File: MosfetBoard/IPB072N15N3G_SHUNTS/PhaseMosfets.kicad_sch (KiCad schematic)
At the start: 26 parts, among them J1 DRIVER1, J4 PhaseConn, Q1 IPB072N15N3G, Q2 IPB072N15N3G, Q4 IPB072N15N3G, Q5 IPB072N15N3G

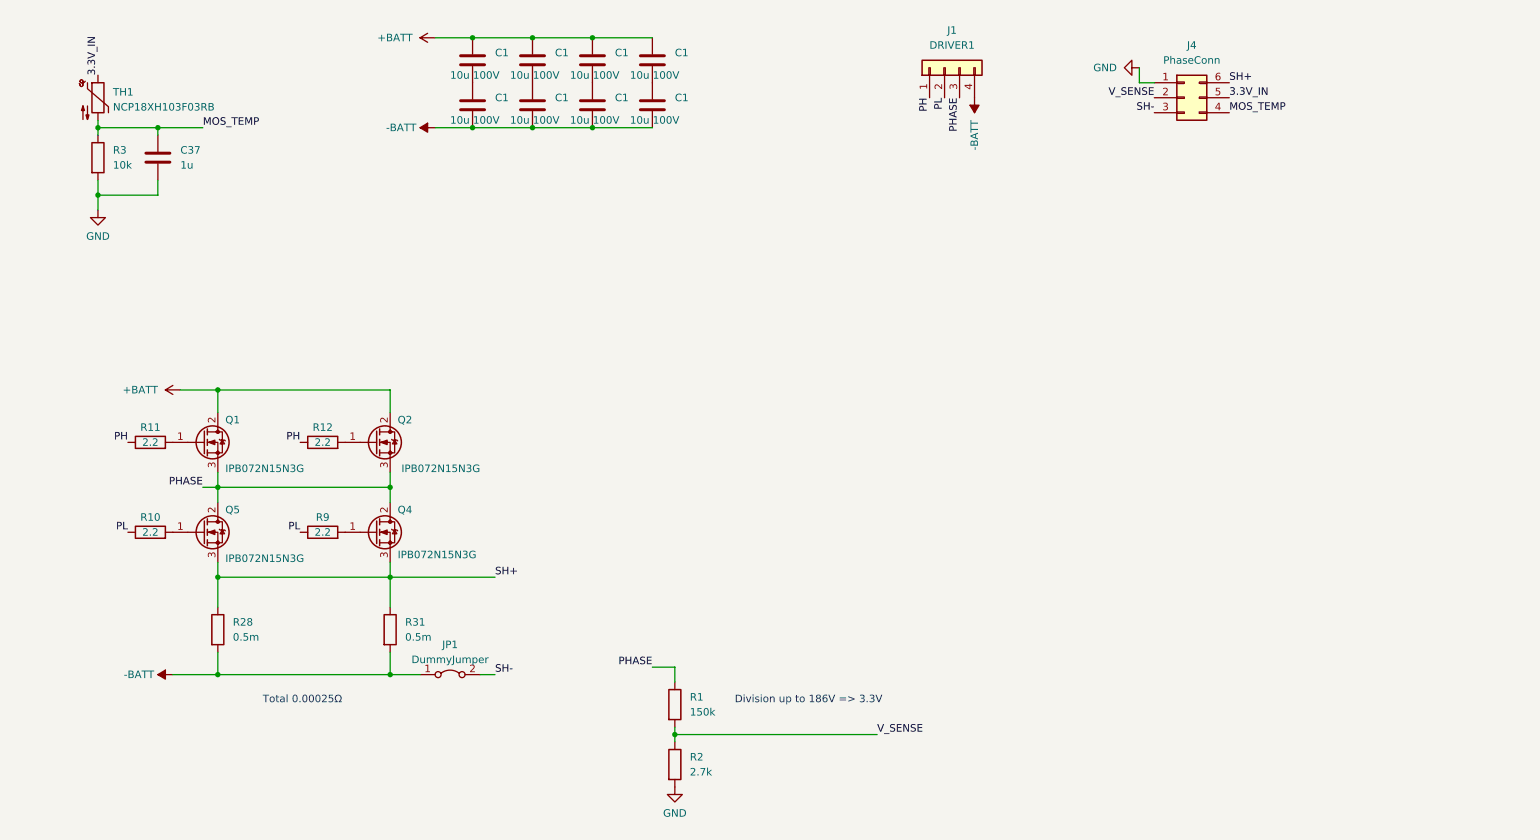
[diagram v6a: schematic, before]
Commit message: v2.8.0 - Small Hall sensors
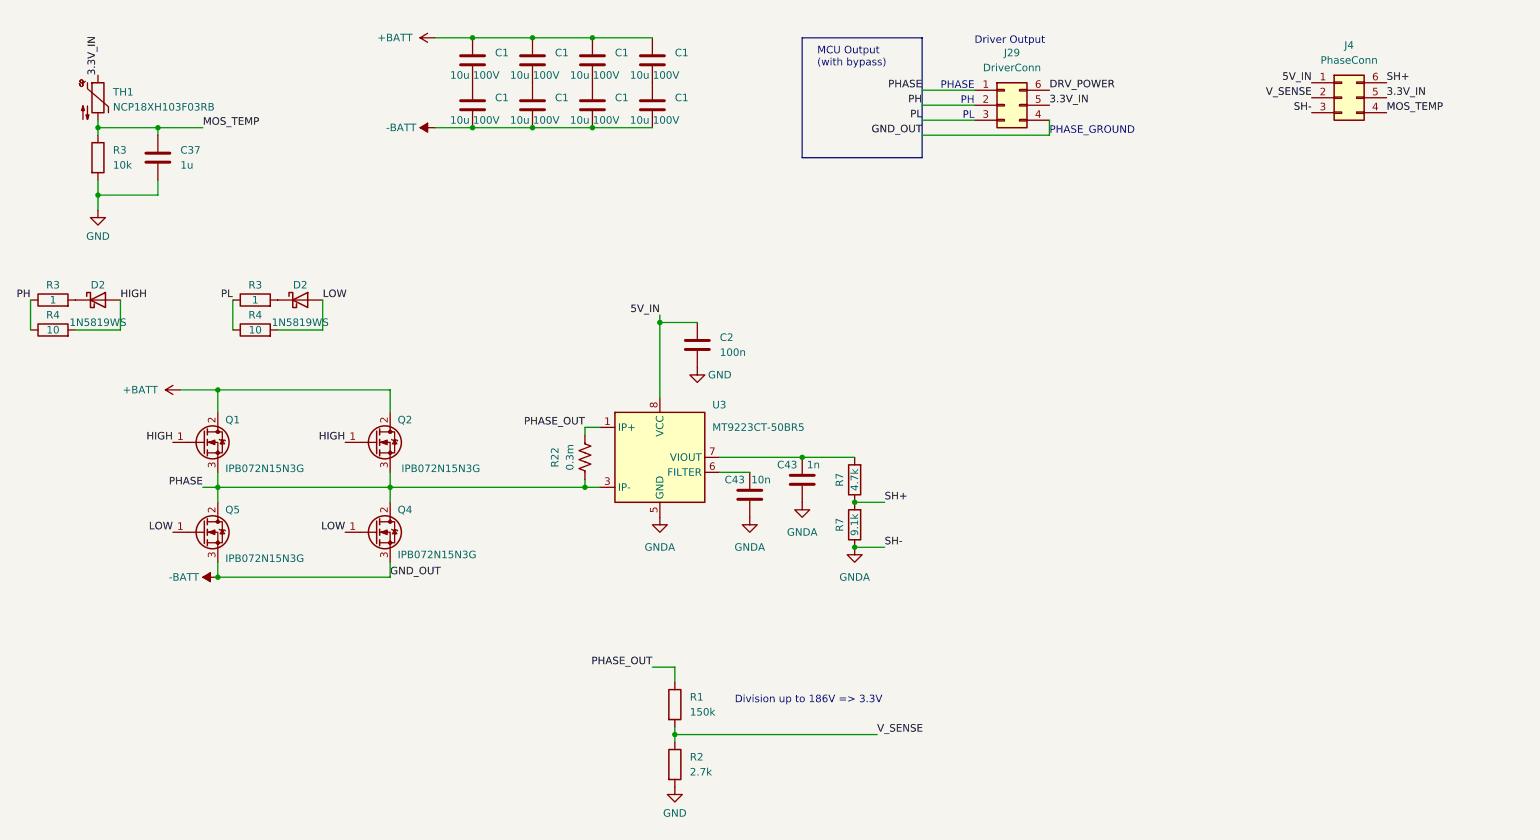
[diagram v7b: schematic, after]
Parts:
- removed J1: DRIVER1, Connector_PinSocket_2.54mm:PinSocket_2x02_P2.54mm_Vertical_SMD, symbol Connector_Generic:Conn_01x04
- removed JP1: DummyJumper, GigaVescLibs:SolderJumper0.3mm, symbol Jumper:Jumper_2_Bridged
- removed R10, R11, R12, R9: 2.2, Resistor_SMD:R_0603_1608Metric, symbol Device:R
- removed R28, R31: 0.5m, Resistor_SMD:R_2512_6332Metric, symbol Device:R
- added C2: 100n, GigaVescLibs:C_0603_1608Metric_L, symbol Device:C
- added C43: 10n, GigaVescLibs:C_0603_1608Metric_L, symbol Device:C
- added C43: 1n, GigaVescLibs:C_0603_1608Metric_L, symbol Device:C
- added D2 (x2): 1N5819WS, Diode_SMD:D_SOD-323, symbol Device:D_Schottky
- added J29: DriverConn, Connector_PinSocket_2.54mm:PinSocket_2x03_P2.54mm_Vertical_SMD, symbol Connector_Generic:Conn_02x03_Counter_Clockwise
- added R22: 0.3m, Resistor_SMD:R_2512_6332Metric, symbol Device:R_US
- added R3 (x2): 1, Resistor_SMD:R_0603_1608Metric, symbol Device:R
- added R4 (x2): 10, Resistor_SMD:R_0603_1608Metric, symbol Device:R
- added R7: 4.7k, Resistor_SMD:R_0603_1608Metric, symbol Device:R
- added R7: 9.1k, Resistor_SMD:R_0603_1608Metric, symbol Device:R
- added U3: MT9223CT-50BR5, Package_SO:SOP-8_3.9x4.9mm_P1.27mm, symbol Sensor_Current:ACS725xLCTR-50AB
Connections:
- net -BATT: now also Q4.3 (S), Q5.3 (S), J29.4 (Pin_4)
- net 3.3V_IN: now also J29.5 (Pin_5)
- net GND: now also C2.1; no longer J4.1 (Pin_1)
- net PH: now also J29.2 (Pin_2), R3.1, R4.1
- net PHASE: now also J29.1 (Pin_1), R22.1, U3.3 (IP-), U3.4 (IP-); no longer R1.1
- net PL: now also J29.3 (Pin_3), R3.1, R4.1
- net SH+: now also R7.1, R7.2; no longer Q4.3 (S), Q5.3 (S)
- net LOW: now reaches Q5.1 (G)
- net LOW: now also Q4.1 (G), D2.2 (A), R4.2
- net HIGH: now reaches Q2.1 (G)
- net HIGH: now also Q1.1 (G), D2.2 (A), R4.2
- net SH- renamed GNDA
- net GNDA: now also C43.2, C43.2, R7.1, U3.5 (GND)
- new net: D2.1 (K), R3.2 (x2)
- new net: C43.1, R7.2, U3.7 (VIOUT)
- new net: C43.1, U3.6 (FILTER)
- new net 5V_IN: C2.2, J4.1 (Pin_1), U3.8 (VCC)
- new net DRV_POWER: J29.6 (Pin_6)
- new net PHASE_OUT: R1.1, R22.2, U3.1 (IP+), U3.2 (IP+)
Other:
- note added: "Driver Output"
- note added: "MCU Output (with bypass)"
- note added: "PH"
- note added: "PHASE"
- note added: "PHASE_GROUND"
- note added: "PL"
- note removed: "Total 0.00025Ω"
- moved on the sheet: J4

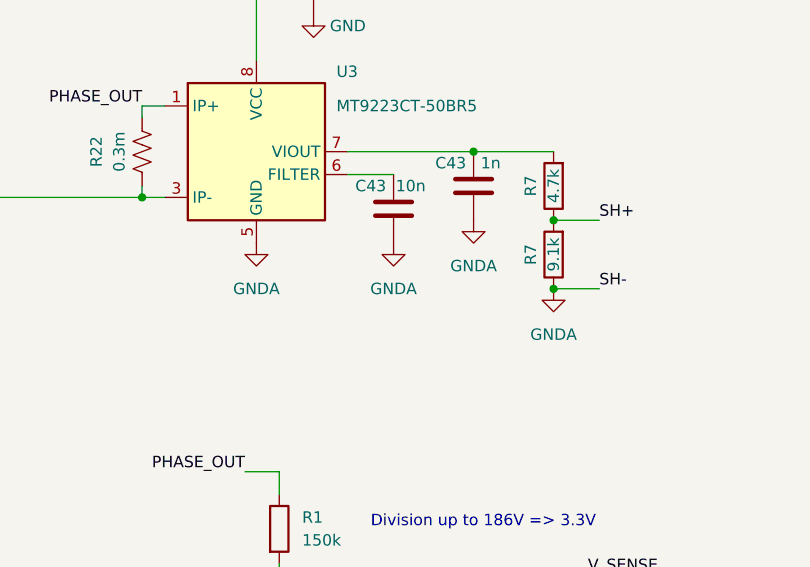
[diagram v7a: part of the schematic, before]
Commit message: v2.8.0 - Small Hall sensors
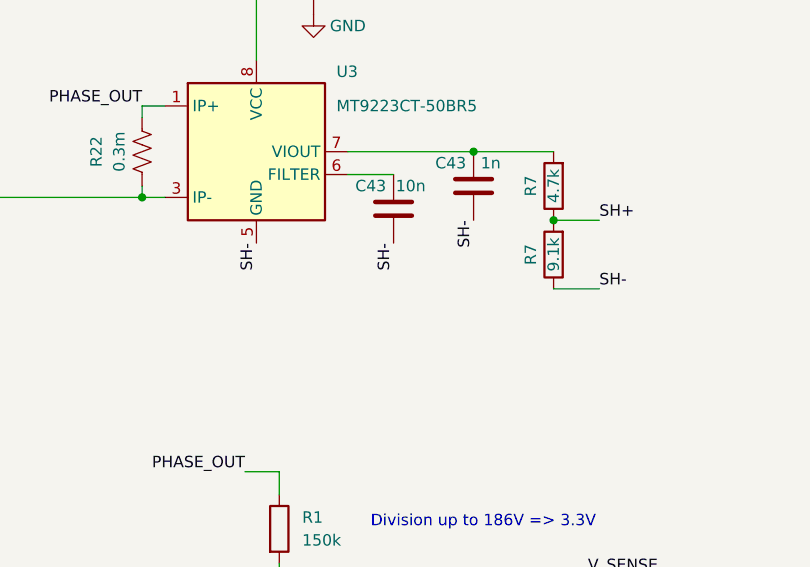
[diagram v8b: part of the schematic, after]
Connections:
- net GNDA renamed SH-
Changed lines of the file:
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@@
   (junction (at 55.88 102.87) (diameter 0) (color 0 0 0 0)
-  )
-  (junction (at 163.83 113.03) (diameter 0) (color 0 0 0 0)
   )
   (junction (at 133.35 144.78) (diameter 0) (color 0 0 0 0)
@@
     (effects (font (size 1.27 1.27)) (justify left bottom))
   )
+  (label "SH-" (at 146.05 107.95 270) (fields_autoplaced)
+    (effects (font (size 1.27 1.27)) (justify right bottom))
+  )
   (label "LOW" (at 77.47 110.49 180) (fields_autoplaced)
     (effects (font (size 1.27 1.27)) (justify right bottom))
@@
   )
   (label "PL" (at 58.42 71.12 180) (fields_autoplaced)
+    (effects (font (size 1.27 1.27)) (justify right bottom))
+  )
+  (label "SH-" (at 154.94 105.41 270) (fields_autoplaced)
     (effects (font (size 1.27 1.27)) (justify right bottom))
   )
@@
   (label "MOS_TEMP" (at 53.34 41.91 0) (fields_autoplaced)
     (effects (font (size 1.27 1.27)) (justify left bottom))
+  )
+  (label "SH-" (at 130.81 107.95 270) (fields_autoplaced)
+    (effects (font (size 1.27 1.27)) (justify right bottom))
   )
   (label "MOS_TEMP" (at 254 39.37 0) (fields_autoplaced)
@@
     )
   )
-  (symbol (lib_id "power:GNDA") (at 154.94 105.41 0) (unit 1)
-    (in_bom yes) (on_board yes) (dnp no) (fields_autoplaced)
-    (property "Reference" "#PWR012" (at 154.94 111.76 0)
-      (effects (font (size 1.27 1.27)) hide)
-    )
-    (property "Value" "GNDA" (at 154.94 110.49 0)
-      (effects (font (size 1.27 1.27)))
-    )
-    (property "Footprint" "" (at 154.94 105.41 0)
-      (effects (font (size 1.27 1.27)) hide)
-    )
-    (property "Datasheet" "" (at 154.94 105.41 0)
-      (effects (font (size 1.27 1.27)) hide)
-    )
-    (pin "1")
-    (instances
-      (project "IPB072N15N3G_SHUNTS"
-        (path "/8a7bb686-c87a-43a6-b3d4-d988e8a2213f/3d569e84-87d6-4696-b0ce-a4e576394c1a"
-          (reference "#PWR012") (unit 1)
-        )
-        (path "/8a7bb686-c87a-43a6-b3d4-d988e8a2213f/db7451b3-bde8-4d72-ba04-6d13b057caad"
-          (reference "#PWR022") (unit 1)
-        )
-        (path "/8a7bb686-c87a-43a6-b3d4-d988e8a2213f/ccaed507-63cb-4563-a707-3e0cba7d2643"
-          (reference "#PWR030") (unit 1)
-        )
-      )
-    )
-  )
   (symbol (lib_id "power:GND") (at 35.56 55.88 0) (unit 1)
     (in_bom yes) (on_board yes) (dnp no) (fields_autoplaced)
@@
         (path "/8a7bb686-c87a-43a6-b3d4-d988e8a2213f/ccaed507-63cb-4563-a707-3e0cba7d2643"
           (reference "#PWR052") (unit 1)
-        )
-      )
-    )
-  )
-  (symbol (lib_id "power:GNDA") (at 130.81 107.95 0) (unit 1)
-    (in_bom yes) (on_board yes) (dnp no) (fields_autoplaced)
-    (property "Reference" "#PWR01" (at 130.81 114.3 0)
-      (effects (font (size 1.27 1.27)) hide)
-    )
-    (property "Value" "GNDA" (at 130.81 113.03 0)
-      (effects (font (size 1.27 1.27)))
-    )
-    (property "Footprint" "" (at 130.81 107.95 0)
-      (effects (font (size 1.27 1.27)) hide)
-    )
-    (property "Datasheet" "" (at 130.81 107.95 0)
-      (effects (font (size 1.27 1.27)) hide)
-    )
-    (pin "1")
-    (instances
-      (project "IPB072N15N3G_SHUNTS"
-        (path "/8a7bb686-c87a-43a6-b3d4-d988e8a2213f/3d569e84-87d6-4696-b0ce-a4e576394c1a"
-          (reference "#PWR01") (unit 1)
-        )
-        (path "/8a7bb686-c87a-43a6-b3d4-d988e8a2213f/db7451b3-bde8-4d72-ba04-6d13b057caad"
-          (reference "#PWR015") (unit 1)
-        )
-        (path "/8a7bb686-c87a-43a6-b3d4-d988e8a2213f/ccaed507-63cb-4563-a707-3e0cba7d2643"
-          (reference "#PWR027") (unit 1)
         )
       )
@@
     )
   )
-  (symbol (lib_id "power:GNDA") (at 163.83 113.03 0) (unit 1)
-    (in_bom yes) (on_board yes) (dnp no) (fields_autoplaced)
-    (property "Reference" "#PWR014" (at 163.83 119.38 0)
-      (effects (font (size 1.27 1.27)) hide)
-    )
-    (property "Value" "GNDA" (at 163.83 118.11 0)
-      (effects (font (size 1.27 1.27)))
-    )
-    (property "Footprint" "" (at 163.83 113.03 0)
-      (effects (font (size 1.27 1.27)) hide)
-    )
-    (property "Datasheet" "" (at 163.83 113.03 0)
-      (effects (font (size 1.27 1.27)) hide)
-    )
-    (pin "1")
-    (instances
-      (project "IPB072N15N3G_SHUNTS"
-        (path "/8a7bb686-c87a-43a6-b3d4-d988e8a2213f/3d569e84-87d6-4696-b0ce-a4e576394c1a"
-          (reference "#PWR014") (unit 1)
-        )
-        (path "/8a7bb686-c87a-43a6-b3d4-d988e8a2213f/db7451b3-bde8-4d72-ba04-6d13b057caad"
-          (reference "#PWR026") (unit 1)
-        )
-        (path "/8a7bb686-c87a-43a6-b3d4-d988e8a2213f/ccaed507-63cb-4563-a707-3e0cba7d2643"
-          (reference "#PWR031") (unit 1)
-        )
-      )
-    )
-  )
   (symbol (lib_id "Device:R") (at 27.94 71.12 90) (unit 1)
     (in_bom yes) (on_board yes) (dnp no)
@@
         )
       )
-    )
-  )
-  (symbol (lib_id "power:GNDA") (at 146.05 107.95 0) (unit 1)
-    (in_bom yes) (on_board yes) (dnp no) (fields_autoplaced)
-    (property "Reference" "#PWR011" (at 146.05 114.3 0)
-      (effects (font (size 1.27 1.27)) hide)
-    )
-    (property "Value" "GNDA" (at 146.05 113.03 0)
-      (effects (font (size 1.27 1.27)))
-    )
-    (property "Footprint" "" (at 146.05 107.95 0)
-      (effects (font (size 1.27 1.27)) hide)
-    )
-    (property "Datasheet" "" (at 146.05 107.95 0)
-      (effects (font (size 1.27 1.27)) hide)
-    )
-    (pin "1")
-    (instances
-      (project "IPB072N15N3G_SHUNTS"
-        (path "/8a7bb686-c87a-43a6-b3d4-d988e8a2213f/3d569e84-87d6-4696-b0ce-a4e576394c1a"
-          (reference "#PWR011") (unit 1)
-        )
-        (path "/8a7bb686-c87a-43a6-b3d4-d988e8a2213f/db7451b3-bde8-4d72-ba04-6d13b057caad"
-          (reference "#PWR021") (unit 1)
-        )
-        (path "/8a7bb686-c87a-43a6-b3d4-d988e8a2213f/ccaed507-63cb-4563-a707-3e0cba7d2643"
-          (reference "#PWR029") (unit 1)
-        )
-      )
